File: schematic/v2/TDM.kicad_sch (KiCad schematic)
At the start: 17 parts, among them J18 LCD_display, U5 24LC256-I_SN, U6 BME280, U8 24LC256-I_SN, U9 NUCLEO-F446RE

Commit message: no errors in the ERC!
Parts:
- removed U5, U8: 24LC256-I_SN, 24LC256-I_SN:SOIC127P600X175-8N, symbol 24LC256-I_SN:24LC256-I_SN
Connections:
- net GND: now also U6.1 (GND)
- no-connect marks 0 -> 5
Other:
- added sheet TDM_crashtable (TDM_crashtable.kicad_sch)
- moved on the sheet: J18

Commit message: time to start routing?
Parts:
- added R51, R52, R53, R54, R55, R57: 10k, Resistor_SMD:R_0805_2012Metric_Pad1.20x1.40mm_HandSolder, symbol Device:R
- added TH2, TH3, TH4, TH5, TH6, TH7: 10k, OptoDevice:R_LDR_4.9x4.2mm_P2.54mm_Vertical, symbol Device:Thermistor
- added unit 1 of U9
- J18: footprint Connector_PinHeader_1.00mm:PinHeader_1x04_P1.00mm_Vertical_SMD_Pin1Left -> Connector_PinHeader_1.00mm:PinHeader_1x04_P1.00mm_Horizontal
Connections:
- net TDM_VDD is gone; now on net 5V_TDM: J18.1 (Pin_1), R15.2, R19.2, U6.8 (VDD)
- net 5V_TDM: now also R51.2, R52.2, R53.2, R54.2, R55.2, R57.2
- net GND: now also TH2.1, TH3.1, TH4.1, TH5.1, TH6.1, TH7.1
- net at R19.1, TH1.2: no longer U9.CN10_19 (PC7)
- new net: R53.1, TH4.2, U9.CN7_36 (PC1/PB9)
- new net: R51.1, TH2.2
- new net: R52.1, TH3.2
- new net: R55.1, TH6.2, U9.CN7_34 (PB0)
- new net: U9.CN7_19 (CN7_GND), U9.CN7_20 (CN7_GND), U9.CN7_22 (CN7_GND), U9.CN7_8 (CN7_GND)
- new net: R57.1, TH7.2, U9.CN7_32 (PA4)
- new net: R54.1, TH5.2, U9.CN7_38 (PC0/PB8)
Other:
- removed sheet TDM_debug
- moved on the sheet: D1, D2, D3, D4, J18, R11, R12, R15, R16, R17, R18, R19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

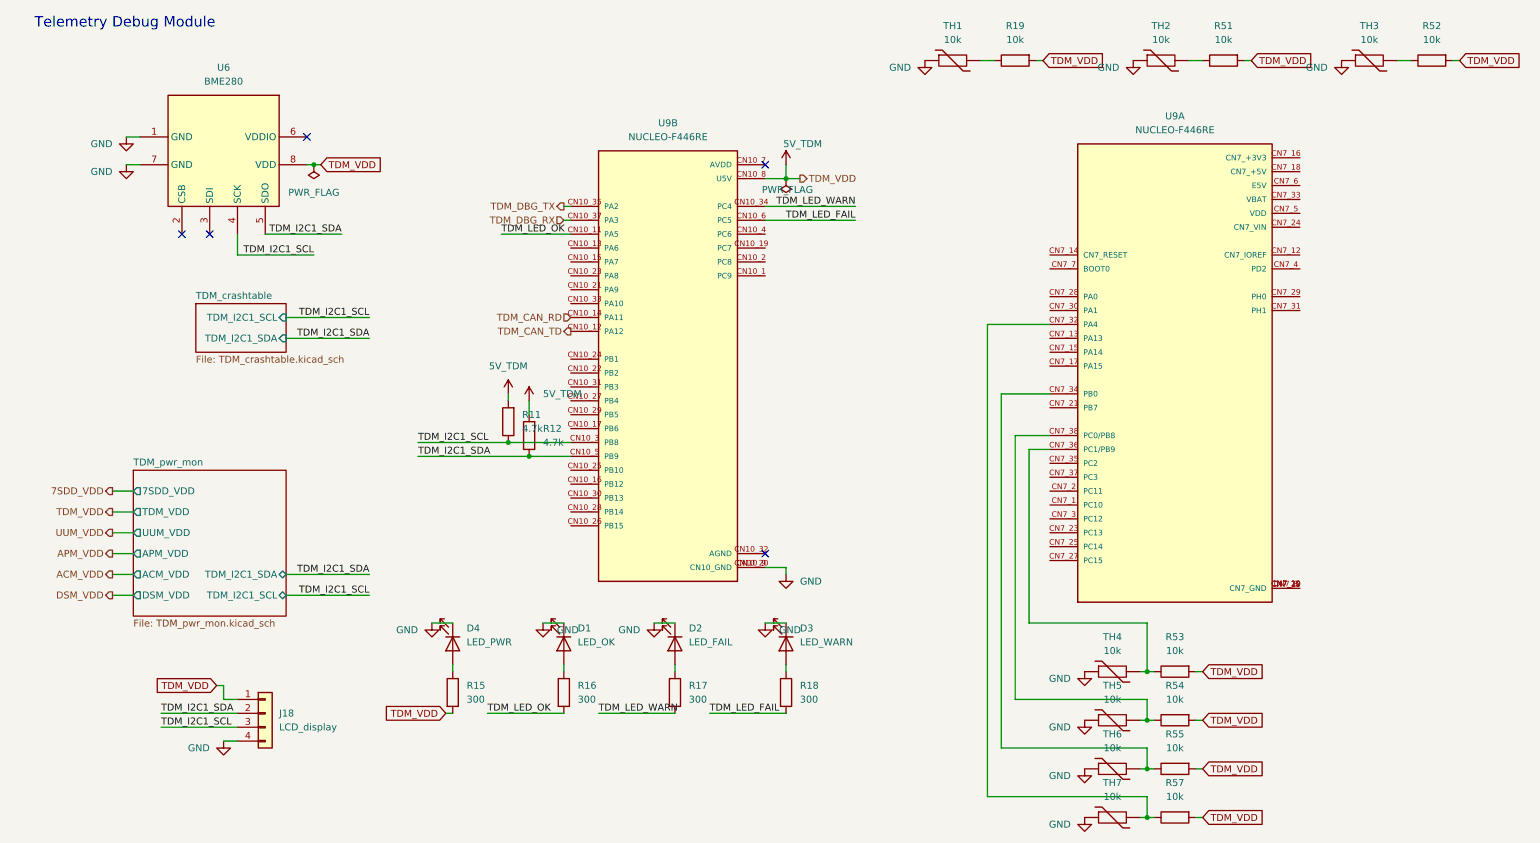
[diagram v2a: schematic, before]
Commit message: gonna throw auto route on. I think I have enough put together for now
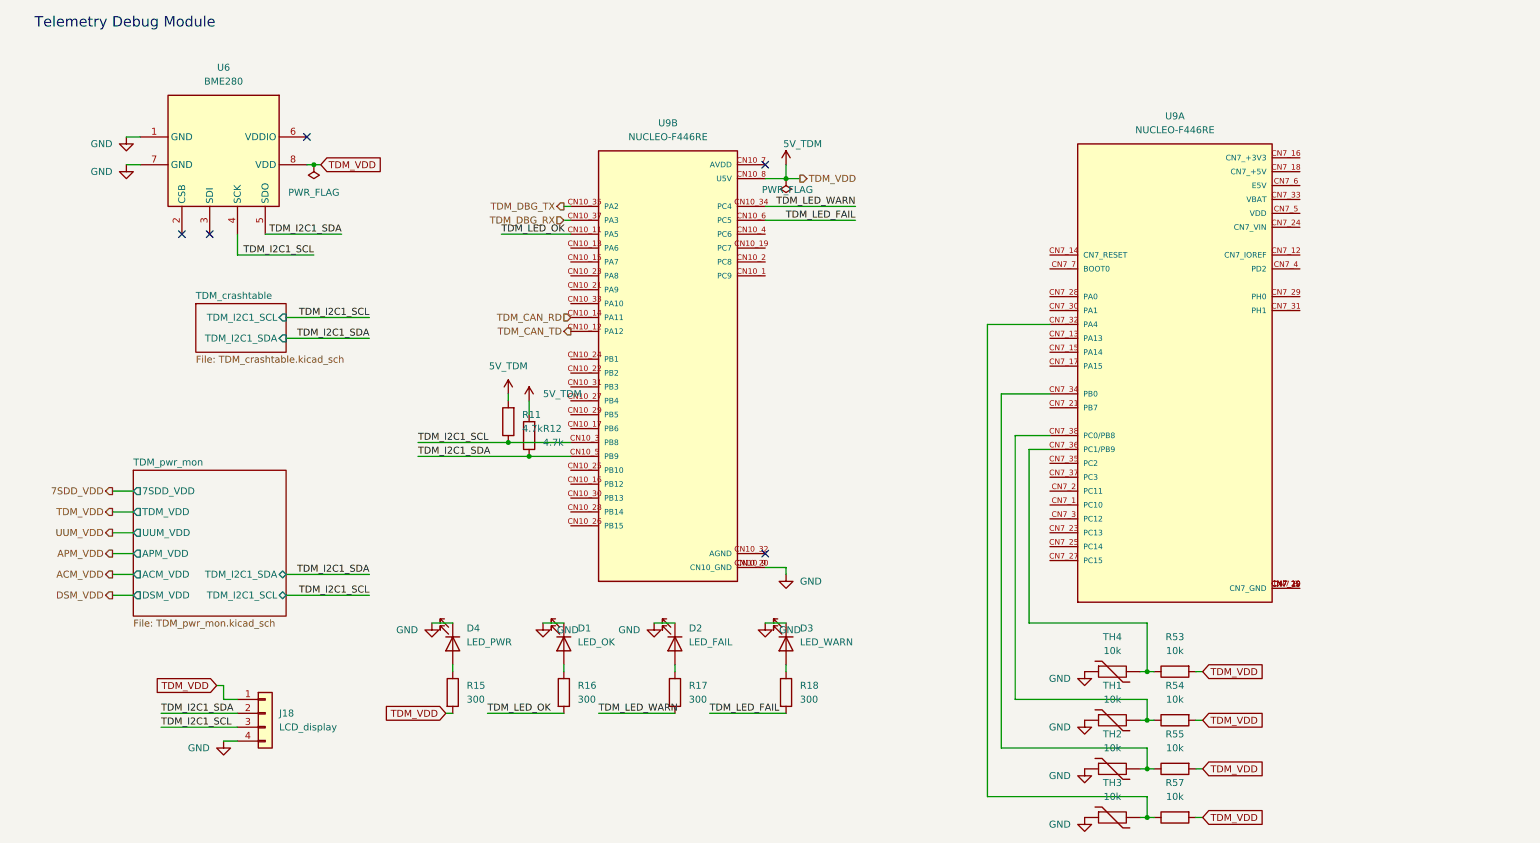
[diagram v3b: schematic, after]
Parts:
- removed R19, R51, R52: 10k, Resistor_SMD:R_0805_2012Metric_Pad1.20x1.40mm_HandSolder, symbol Device:R
- removed TH5, TH6, TH7: 10k, OptoDevice:R_LDR_4.9x4.2mm_P2.54mm_Vertical, symbol Device:Thermistor
- TH1, TH2, TH3, TH4: footprint OptoDevice:R_LDR_4.9x4.2mm_P2.54mm_Vertical -> Package_TO_SOT_THT:Heraeus_TO-92-2
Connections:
- net at TH2.2: now also R55.1, U9.CN7_34 (PB0)
- net at TH3.2: now also R57.1, U9.CN7_32 (PA4)
- net at TH1.2: now also R54.1, U9.CN7_38 (PC0/PB8)

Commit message: schematic updates, no errors at least. running DRC on pcb
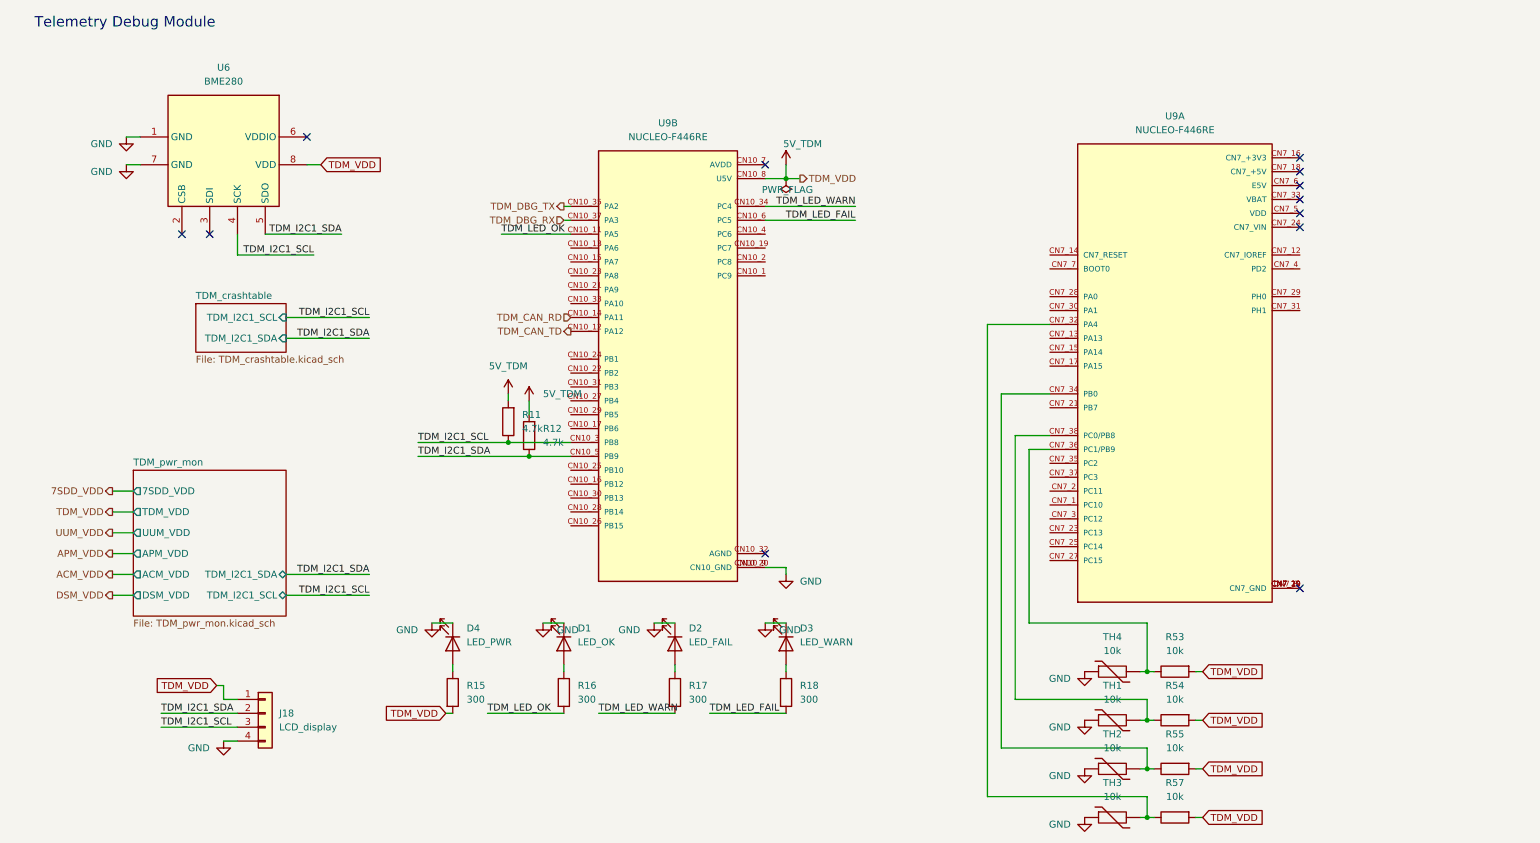
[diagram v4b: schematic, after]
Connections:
- no-connect marks 5 -> 12
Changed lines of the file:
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@@
 		(color 0 0 0 0)
 	)
-	(junction
-		(at 67.31 41.91)
-		(diameter 0)
-		(color 0 0 0 0)
+	(no_connect
+		(at 247.65 43.18)
+	)
+	(no_connect
+		(at 247.65 53.34)
 	)
 	(no_connect
@@
 	)
 	(no_connect
+		(at 247.65 119.38)
+	)
+	(no_connect
 		(at 66.04 36.83)
+	)
+	(no_connect
+		(at 247.65 40.64)
+	)
+	(no_connect
+		(at 247.65 50.8)
 	)
 	(no_connect
@@
 	)
 	(no_connect
+		(at 247.65 48.26)
+	)
+	(no_connect
+		(at 247.65 45.72)
+	)
+	(no_connect
 		(at 48.26 54.61)
 	)
@@
 	(wire
 		(pts
-			(xy 67.31 41.91) (xy 68.58 41.91)
+			(xy 66.04 41.91) (xy 68.58 41.91)
 		)
 		(stroke
@@
 		(pts
 			(xy 198.12 93.98) (xy 198.12 125.73)
-		)
-		(stroke
-			(width 0)
-			(type default)
-		)
-	)
-	(wire
-		(pts
-			(xy 66.04 41.91) (xy 67.31 41.91)
 		)
 		(stroke
@@
 					(unit 1)
 				)
-			)
-		)
-	)
-	(symbol
-		(lib_id "power:PWR_FLAG")
-		(at 67.31 41.91 180)
-		(unit 1)
-		(exclude_from_sim no)
-		(in_bom yes)
-		(on_board yes)
-		(dnp no)
-		(fields_autoplaced yes)
-		(property "Reference" "#FLG011"
-			(at 67.31 43.815 0)
-			(effects
-				(font
-					(size 1.27 1.27)
-				)
-				(hide yes)
-			)
-		)
-		(property "Value" "PWR_FLAG"
-			(at 67.31 46.99 0)
-			(effects
-				(font
-					(size 1.27 1.27)
-				)
-			)
-		)
-		(property "Footprint" ""
-			(at 67.31 41.91 0)
-			(effects
-				(font
-					(size 1.27 1.27)
-				)
-				(hide yes)
-			)
-		)
-		(property "Datasheet" "~"
-			(at 67.31 41.91 0)
-			(effects
-				(font
-					(size 1.27 1.27)
-				)
-				(hide yes)
-			)
-		)
-		(property "Description" "Special symbol for telling ERC where power comes from"
-			(at 67.31 41.91 0)
-			(effects
-				(font
-					(size 1.27 1.27)
-				)
-				(hide yes)
-			)
-		)
-		(pin "1"
-		)
-		(instances
-			(project ""
-				(path "/fe7b15e9-f0ed-4338-9f03-dd7651dace13/442c7b41-f8c0-48e5-8b80-63d502cac366"
-					(reference "#FLG011")
-					(unit 1)
-				)

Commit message: hmmm figuring out filter module right now
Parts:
- added R19: 10k, Resistor_SMD:R_0805_2012Metric_Pad1.20x1.40mm_HandSolder, symbol Device:R
- added TH5: 10k, Package_TO_SOT_THT:Heraeus_TO-92-2, symbol Device:Thermistor
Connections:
- net 5V_TDM: now also R19.2
- net GND: now also TH5.1
- new net: R19.1, TH5.2
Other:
- moved on the sheet: R53, R54, R55, R57, TH1, TH2, TH3, TH4, U9A
